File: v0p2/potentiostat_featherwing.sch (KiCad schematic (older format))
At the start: 20 parts, among them J1 Screw_Terminal_01x03, J2 Conn_01x03, J3 Conn_01x02, U1 feather_wing, U2 ADG702, U3 MCP6004

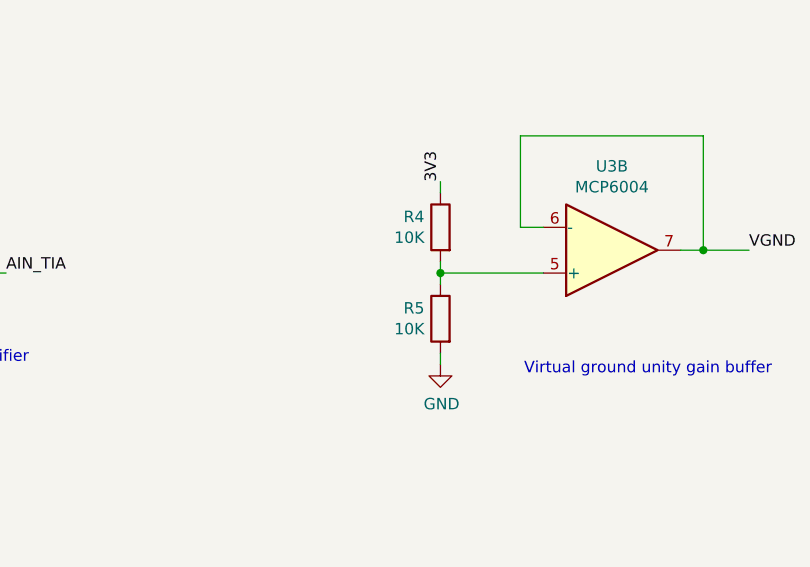
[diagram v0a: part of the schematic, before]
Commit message: Created version 0.2 of the design.  Changed op amps. Added switch. Added ground test point.
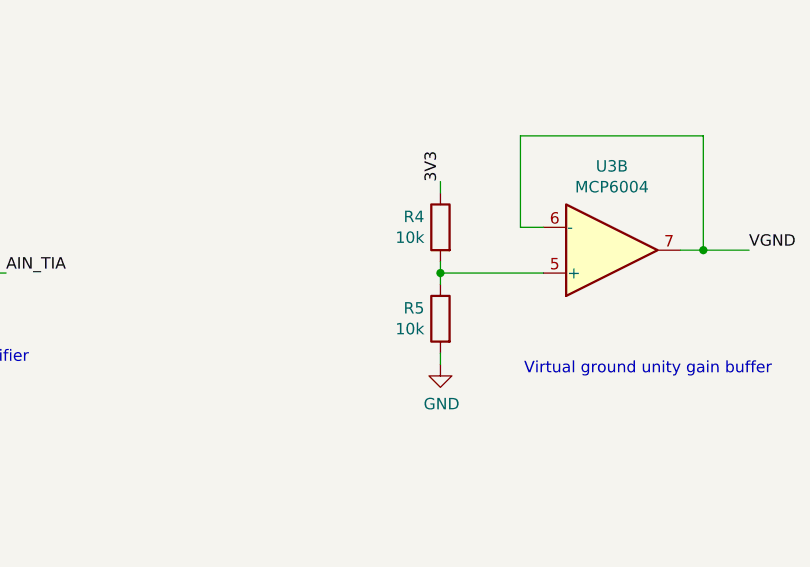
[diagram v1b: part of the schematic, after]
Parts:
- R4, R5: value 10K -> 10k
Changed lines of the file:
@@
 P 8300 4500
 F 0 "R5" H 8370 4546 50  0000 L CNN
-F 1 "10K" H 8370 4455 50  0000 L CNN
+F 1 "10k" H 8370 4455 50  0000 L CNN
 F 2 "Resistor_SMD:R_0603_1608Metric_Pad1.05x0.95mm_HandSolder" V 8230 4500 50  0001 C CNN
 F 3 "~" H 8300 4500 50  0001 C CNN
@@
 P 8300 4100
 F 0 "R4" H 8370 4146 50  0000 L CNN
-F 1 "10K" H 8370 4055 50  0000 L CNN
+F 1 "10k" H 8370 4055 50  0000 L CNN
 F 2 "Resistor_SMD:R_0603_1608Metric_Pad1.05x0.95mm_HandSolder" V 8230 4100 50  0001 C CNN
 F 3 "~" H 8300 4100 50  0001 C CNN

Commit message: Minor modifications for schematic - no substantive changes. Remade gerber files for v0p2_r2.
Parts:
- U2: symbol ADG702:ADG702 -> potentiostat_featherwing-rescue:ADG702-ADG702
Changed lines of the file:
@@
 Connection ~ 6050 1950
 $Comp
-L ADG702:ADG702 U2
+L potentiostat_featherwing-rescue:ADG702-ADG702 U2
 U 1 1 5E4C7935
 P 7050 1950
